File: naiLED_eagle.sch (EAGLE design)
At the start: 8 parts, among them IC1 TCS3414, U2 24LC00T-I/OT, U3 ATTINY25-20SSU

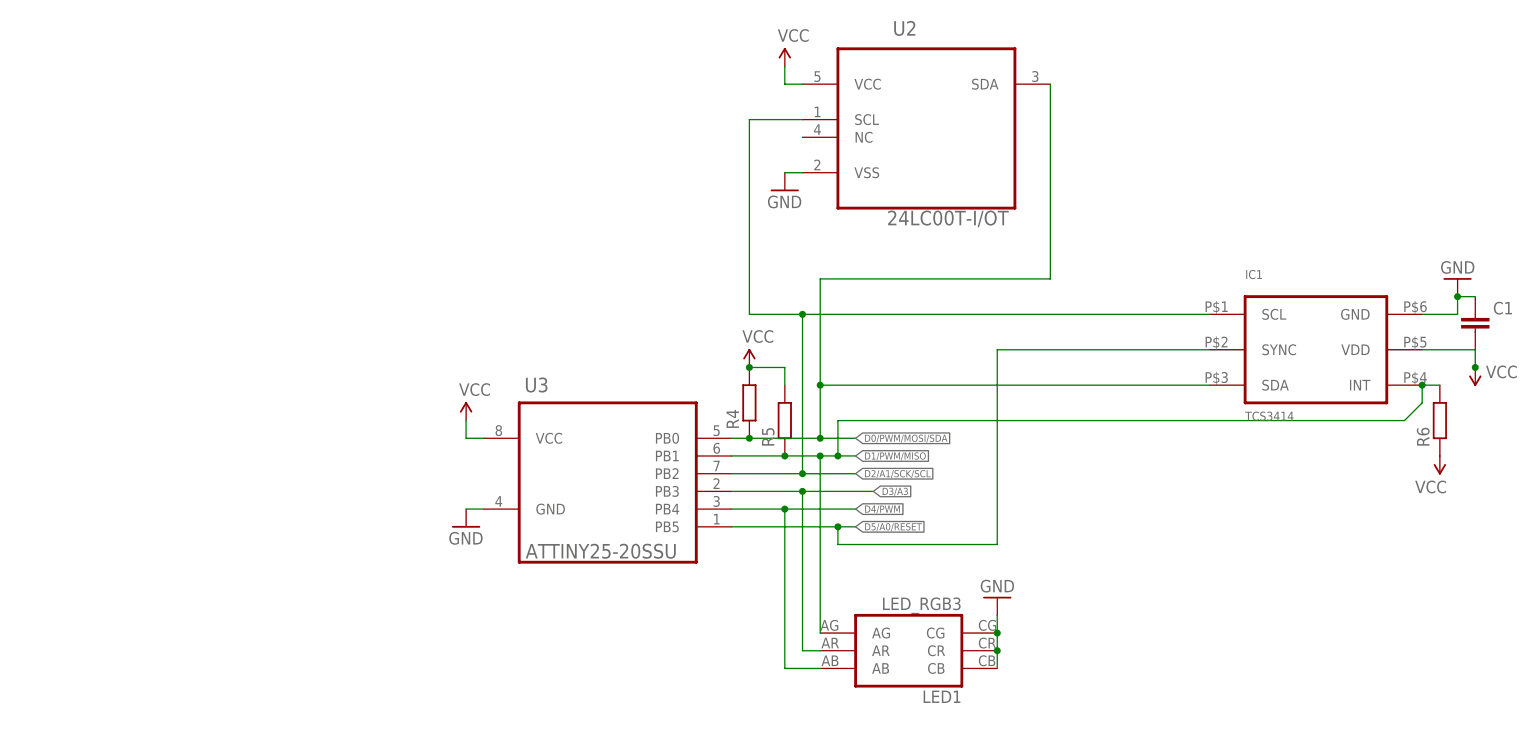
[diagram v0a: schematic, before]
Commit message: added library
ripup all , changed LED to CLPP4 and added resistors
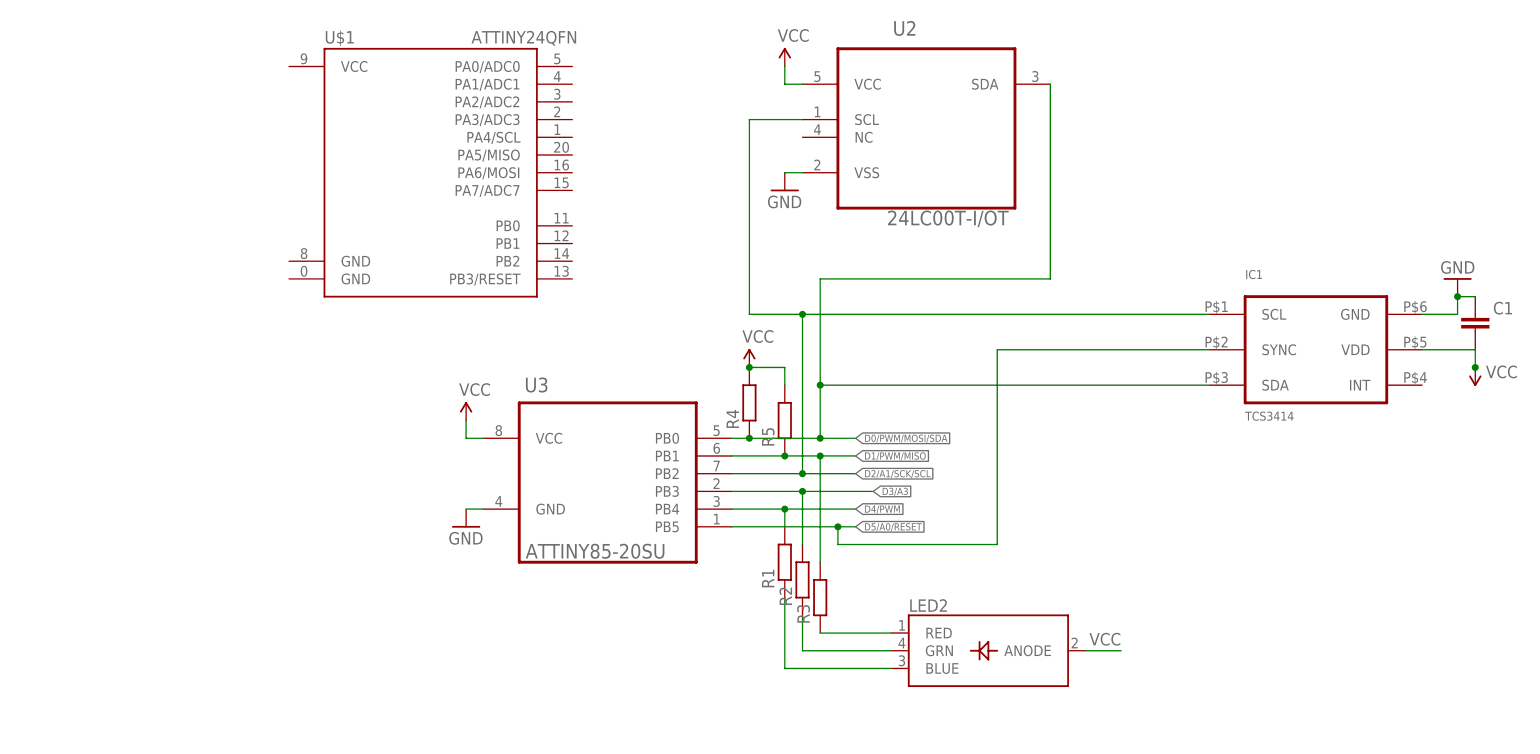
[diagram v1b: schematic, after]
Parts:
- removed LED1: LED_RGB3, dp_devices:LED_RGB3
- removed R6: (no value), dp_devices:RESISTOR-0402
- added LED2: (no value), microbuilder:LED_RGB_PLCC4
- added R1, R2, R3: (no value), dp_devices:RESISTOR-0402
- added U$1: ATTINY24QFN, SparkFun-DigitalIC:ATTINY24QFN
- U3: value ATTINY25-20SSU -> ATTINY85-20SU; device yair_r:ATTINY25-20SSU -> nld:ATTINY85-20SU
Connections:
- new net N$1: LED2.RED, R3.1
- new net N$2: LED2.GRN, R2.1
- new net N$3: LED2.BLUE, R1.1
- net D1/PWM/MISO: now also R3.2; no longer IC1.INT, LED1.AG, R6.2
- net D3/A3: now also R2.2; no longer LED1.AR
- net D4/PWM: now also R1.2; no longer LED1.AB
- net GND: no longer LED1.CB, LED1.CG, LED1.CR
- net VCC: now also LED2.ANODE; no longer R6.1
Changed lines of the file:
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@@
 <?xml version="1.0" encoding="utf-8"?>
 <!DOCTYPE eagle SYSTEM "eagle.dtd">
-<eagle version="6.4">
+<eagle version="7.1.0">
 <drawing>
 <settings>
@@
 <layer number="54" name="bGND_GNDA" color="7" fill="1" visible="no" active="no"/>
 <layer number="56" name="wert" color="7" fill="1" visible="no" active="no"/>
+<layer number="90" name="Modules" color="5" fill="1" visible="yes" active="yes"/>
 <layer number="91" name="Nets" color="2" fill="1" visible="yes" active="yes"/>
 <layer number="92" name="Busses" color="1" fill="1" visible="yes" active="yes"/>
@@
 <layer number="107" name="BD-Top" color="7" fill="1" visible="yes" active="yes"/>
 <layer number="108" name="centerline" color="7" fill="1" visible="yes" active="yes"/>
+<layer number="109" name="tBPL" color="7" fill="1" visible="yes" active="yes"/>
+<layer number="110" name="bBPL" color="7" fill="1" visible="yes" active="yes"/>
+<layer number="111" name="MPL" color="7" fill="1" visible="yes" active="yes"/>
+<layer number="112" name="tSilk" color="7" fill="1" visible="yes" active="yes"/>
 <layer number="116" name="Patch_BOT" color="7" fill="1" visible="yes" active="yes"/>
+<layer number="118" name="Rect_Pads" color="7" fill="1" visible="no" active="no"/>
 <layer number="121" name="_tsilk" color="7" fill="1" visible="yes" active="yes"/>
 <layer number="122" name="_bsilk" color="7" fill="1" visible="yes" active="yes"/>
+<layer number="123" name="tTestmark" color="7" fill="1" visible="no" active="yes"/>
+<layer number="124" name="bTestmark" color="7" fill="1" visible="no" active="yes"/>
 <layer number="125" name="_tNames" color="7" fill="1" visible="yes" active="yes"/>
+<layer number="126" name="_bNames" color="7" fill="1" visible="yes" active="yes"/>
+<layer number="127" name="_tValues" color="7" fill="1" visible="yes" active="yes"/>
+<layer number="128" name="_bValues" color="7" fill="1" visible="yes" active="yes"/>
 <layer number="131" name="prix" color="7" fill="1" visible="yes" active="yes"/>
 <layer number="132" name="test" color="7" fill="1" visible="yes" active="yes"/>
 <layer number="144" name="Drill_legend" color="7" fill="1" visible="yes" active="yes"/>
 <layer number="151" name="HeatSink" color="7" fill="1" visible="yes" active="yes"/>
+<layer number="152" name="_bDocu" color="7" fill="1" visible="yes" active="yes"/>
 <layer number="199" name="Contour" color="7" fill="1" visible="yes" active="yes"/>
 <layer number="200" name="200bmp" color="7" fill="1" visible="yes" active="yes"/>
@@
 <layer number="223" name="223bmp" color="24" fill="1" visible="no" active="no"/>
 <layer number="224" name="224bmp" color="25" fill="1" visible="no" active="no"/>
+<layer number="248" name="Housing" color="7" fill="1" visible="yes" active="yes"/>
+<layer number="249" name="Edge" color="7" fill="1" visible="yes" active="yes"/>
 <layer number="250" name="Descript" color="7" fill="1" visible="yes" active="yes"/>
 <layer number="251" name="SMDround" color="7" fill="1" visible="yes" active="yes"/>
@@
 <parts>
 <part name="U2" library="Microchip-24LCxxx" deviceset="24LC00T-I/OT" device=""/>
-<part name="U3" library="yair_r" deviceset="ATTINY25-20SSU" device=""/>
-<part name="LED1" library="dp_devices" deviceset="LED_RGB3" device=""/>
-<part name="GND1" library="SparkFun" deviceset="GND" device=""/>
+<part name="U3" library="nld" deviceset="ATTINY85-20SU" device=""/>
 <part name="GND3" library="SparkFun" deviceset="GND" device=""/>
 <part name="P+1" library="SparkFun" deviceset="VCC" device=""/>
@@
 <part name="R4" library="dp_devices" deviceset="RESISTOR" device="-0402"/>
 <part name="R5" library="dp_devices" deviceset="RESISTOR" device="-0402"/>
-<part name="P+5" library="SparkFun" deviceset="VCC" device=""/>
-<part name="R6" library="dp_devices" deviceset="RESISTOR" device="-0402"/>
 <part name="C1" library="dp_devices" deviceset="CAPACITOR_NPOL" device="-0402"/>
+<part name="LED2" library="microbuilder" deviceset="LED_RGB_PLCC4" device=""/>
+<part name="R1" library="dp_devices" deviceset="RESISTOR" device="-0402"/>
+<part name="R2" library="dp_devices" deviceset="RESISTOR" device="-0402"/>
+<part name="R3" library="dp_devices" deviceset="RESISTOR" device="-0402"/>
+<part name="U$1" library="SparkFun-DigitalIC" deviceset="ATTINY24" device="QFN"/>
 </parts>
 <sheets>
@@
 <attribute name="VALUE" x="-11.7856" y="13.2334" size="2.0828" layer="96" ratio="10" rot="SR0"/>
 </instance>
-<instance part="LED1" gate="G$1" x="43.18" y="0" rot="R180"/>
-<instance part="GND1" gate="1" x="55.88" y="7.62" rot="R180"/>
 <instance part="GND3" gate="1" x="-20.32" y="17.78"/>
 <instance part="P+1" gate="1" x="-20.32" y="33.02"/>
@@
 <instance part="R4" gate="G$1" x="20.32" y="35.56" rot="R90"/>
 <instance part="R5" gate="G$1" x="25.4" y="33.02" rot="R90"/>
-<instance part="P+5" gate="1" x="119.38" y="27.94" rot="R180"/>
-<instance part="R6" gate="G$1" x="119.38" y="33.02" rot="R90"/>
 <instance part="C1" gate="C" x="124.46" y="48.26" smashed="yes" rot="R180">
 <attribute name="NAME" x="127" y="48.26" size="1.778" layer="95"/>
 <attribute name="VALUE" x="121.92" y="45.72" size="1.778" layer="96" rot="R180"/>
 </instance>
+<instance part="LED2" gate="G$1" x="53.34" y="0"/>
+<instance part="R1" gate="G$1" x="25.4" y="12.7" rot="R90"/>
+<instance part="R2" gate="G$1" x="27.94" y="10.16" rot="R90"/>
+<instance part="R3" gate="G$1" x="30.48" y="7.62" rot="R90"/>
+<instance part="U$1" gate="G$1" x="-25.4" y="68.58"/>
 </instances>
 <busses>
@@
 </segment>
 <segment>
-<pinref part="R6" gate="G$1" pin="1"/>
-<pinref part="P+5" gate="1" pin="VCC"/>
+<wire x1="68.58" y1="0" x2="73.66" y2="0" width="0.1524" layer="91"/>
+<pinref part="LED2" gate="G$1" pin="ANODE"/>
+<label x="73.66" y="2.54" size="1.778" layer="95" rot="R180"/>
 </segment>
 </net>
 <net name="GND" class="0">
-<segment>
-<wire x1="55.88" y1="-2.54" x2="55.88" y2="0" width="0.1524" layer="91"/>
-<wire x1="55.88" y1="0" x2="55.88" y2="2.54" width="0.1524" layer="91"/>
-<wire x1="55.88" y1="2.54" x2="55.88" y2="5.08" width="0.1524" layer="91"/>
-<junction x="55.88" y="2.54"/>
-<junction x="55.88" y="0"/>
-<pinref part="GND1" gate="1" pin="GND"/>
-<pinref part="LED1" gate="G$1" pin="CB"/>
-<pinref part="LED1" gate="G$1" pin="CR"/>
-<pinref part="LED1" gate="G$1" pin="CG"/>
-</segment>
 <segment>
 <pinref part="GND3" gate="1" pin="GND"/>
@@
 <wire x1="17.78" y1="20.32" x2="25.4" y2="20.32" width="0.1524" layer="91"/>
 <junction x="25.4" y="20.32"/>
-<wire x1="25.4" y1="20.32" x2="25.4" y2="-2.54" width="0.1524" layer="91"/>
-<pinref part="LED1" gate="G$1" pin="AB"/>
-<wire x1="25.4" y1="-2.54" x2="30.48" y2="-2.54" width="0.1524" layer="91"/>
+<wire x1="25.4" y1="20.32" x2="25.4" y2="17.78" width="0.1524" layer="91"/>
+<pinref part="R1" gate="G$1" pin="2"/>
 </segment>
 </net>
@@
 <wire x1="27.94" y1="22.86" x2="38.1" y2="22.86" width="0.1524" layer="91"/>
 <junction x="27.94" y="22.86"/>
-<wire x1="27.94" y1="22.86" x2="27.94" y2="0" width="0.1524" layer="91"/>
-<pinref part="LED1" gate="G$1" pin="AR"/>
-<wire x1="30.48" y1="0" x2="27.94" y2="0" width="0.1524" layer="91"/>
+<wire x1="27.94" y1="22.86" x2="27.94" y2="15.24" width="0.1524" layer="91"/>
+<pinref part="R2" gate="G$1" pin="2"/>
 </segment>
 </net>
@@
 <label x="35.56" y="27.94" size="1.016" layer="95" xref="yes"/>
 <wire x1="25.4" y1="27.94" x2="30.48" y2="27.94" width="0.1524" layer="91"/>
-<wire x1="30.48" y1="27.94" x2="33.02" y2="27.94" width="0.1524" layer="91"/>
-<wire x1="33.02" y1="27.94" x2="35.56" y2="27.94" width="0.1524" layer="91"/>
-<wire x1="30.48" y1="27.94" x2="30.48" y2="2.54" width="0.1524" layer="91"/>
+<wire x1="30.48" y1="27.94" x2="35.56" y2="27.94" width="0.1524" layer="91"/>
+<wire x1="30.48" y1="27.94" x2="30.48" y2="12.7" width="0.1524" layer="91"/>
 <junction x="30.48" y="27.94"/>
 <pinref part="R5" gate="G$1" pin="1"/>
 <junction x="25.4" y="27.94"/>
-<pinref part="LED1" gate="G$1" pin="AG"/>
-<pinref part="IC1" gate="A" pin="INT"/>
-<wire x1="116.84" y1="38.1" x2="119.38" y2="38.1" width="0.1524" layer="91"/>
-<pinref part="R6" gate="G$1" pin="2"/>
-<wire x1="116.84" y1="38.1" x2="116.84" y2="35.56" width="0.1524" layer="91"/>
-<junction x="116.84" y="38.1"/>
-<wire x1="116.84" y1="35.56" x2="114.3" y2="33.02" width="0.1524" layer="91"/>
-<wire x1="114.3" y1="33.02" x2="33.02" y2="33.02" width="0.1524" layer="91"/>
-<wire x1="33.02" y1="33.02" x2="33.02" y2="27.94" width="0.1524" layer="91"/>
-<junction x="33.02" y="27.94"/>
+<pinref part="R3" gate="G$1" pin="2"/>
 </segment>
 </net>
@@
 </segment>
 </net>
+<net name="N$1" class="0">
+<segment>
+<pinref part="R3" gate="G$1" pin="1"/>
+<pinref part="LED2" gate="G$1" pin="RED"/>
+<wire x1="40.64" y1="2.54" x2="30.48" y2="2.54" width="0.1524" layer="91"/>
+</segment>
+</net>
+<net name="N$2" class="0">
+<segment>
+<pinref part="R2" gate="G$1" pin="1"/>
+<wire x1="27.94" y1="5.08" x2="27.94" y2="0" width="0.1524" layer="91"/>
+<pinref part="LED2" gate="G$1" pin="GRN"/>
+<wire x1="40.64" y1="0" x2="27.94" y2="0" width="0.1524" layer="91"/>
+</segment>
+</net>
+<net name="N$3" class="0">
+<segment>
+<pinref part="LED2" gate="G$1" pin="BLUE"/>
+<pinref part="R1" gate="G$1" pin="1"/>
+<wire x1="25.4" y1="7.62" x2="25.4" y2="-2.54" width="0.1524" layer="91"/>
+<wire x1="25.4" y1="-2.54" x2="40.64" y2="-2.54" width="0.1524" layer="91"/>
+</segment>
+</net>

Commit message: working on the at841
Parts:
- removed U$1: ATTINY24QFN, SparkFun-DigitalIC:ATTINY24QFN
- removed U3: ATTINY85-20SU, nld:ATTINY85-20SU
- added GND-TAB, VCC-TAB: (no value), adafruit:PINHD-1X1CB
- added IC2: ATTINY441/841-MU, nld:ATTINY441/841-MU
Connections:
- removed net D0/PWM/MOSI/SDA: IC1.SDA, R4.1, U2.SDA, U3.PB0
- removed net D1/PWM/MISO: R3.2, R5.1, U3.PB1
- removed net D2/A1/SCK/SCL: IC1.SCL, U2.SCL, U3.PB2
- removed net D3/A3: R2.2, U3.PB3
- removed net D4/PWM: R1.2, U3.PB4
- new net MISO: IC2.(PCINT0/ADC0/AREF/MISO)PA0, R5.1
- new net MOSI: IC1.SDA, IC2.(PCINT1/ADC1/AIN00/TOCC0/TXD0/MOSI)PA1, R4.1, U2.SDA
- new net N$4: IC2.(PCINT7/ADC7/TOCC6/ICP1/TXD0/SS)PA7, R1.2
- new net N$5: IC2.(PCINT6/ADC6/ACO1/TOCC5/XCK1/SDA/MOSI)PA6, R2.2
- new net N$6: IC2.(PCINT5/ADC5/ACO0/TOCC4/T2/TXD1/MISO)PA5, R3.2
- new net SCL: IC1.SCL, IC2.(PCINT4/ADC4/AIN11/TOCC3/T1/RXD1/SCL/SCK)PA4, U2.SCL
- net D5/A0/RESET: no longer U3.PB5
- net GND: now also GND-TAB.1, IC2.GND; no longer U3.GND
- net VCC: now also IC2.VCC, VCC-TAB.1; no longer U3.VCC
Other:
- note added: "find me home"
- moved on the sheet: LED2, R1, R2, R3, R4, R5

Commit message: some changes, nothing major
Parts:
- removed GND-TAB, VCC-TAB: (no value), adafruit:PINHD-1X1CB
- removed IC2: ATTINY441/841-MU, nld:ATTINY441/841-MU
- added U$1: ATTINY24QFN, SparkFun-DigitalIC:ATTINY24QFN
- added U3: ATTINY85-20SU, nld:ATTINY85-20SU
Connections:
- removed net MISO: IC2.(PCINT0/ADC0/AREF/MISO)PA0, R5.1
- removed net MOSI: IC1.SDA, IC2.(PCINT1/ADC1/AIN00/TOCC0/TXD0/MOSI)PA1, R4.1, U2.SDA
- removed net N$4: IC2.(PCINT7/ADC7/TOCC6/ICP1/TXD0/SS)PA7, R1.2
- removed net N$5: IC2.(PCINT6/ADC6/ACO1/TOCC5/XCK1/SDA/MOSI)PA6, R2.2
- removed net N$6: IC2.(PCINT5/ADC5/ACO0/TOCC4/T2/TXD1/MISO)PA5, R3.2
- removed net SCL: IC1.SCL, IC2.(PCINT4/ADC4/AIN11/TOCC3/T1/RXD1/SCL/SCK)PA4, U2.SCL
- new net D0/PWM/MOSI/SDA: IC1.SDA, R4.1, U2.SDA, U3.PB0
- new net D1/PWM/MISO: R3.2, R5.1, U3.PB1
- new net D2/A1/SCK/SCL: IC1.SCL, U2.SCL, U3.PB2
- new net D3/A3: R2.2, U3.PB3
- new net D4/PWM: R1.2, U3.PB4
- net D5/A0/RESET: now also U3.PB5
- net GND: now also U3.GND; no longer GND-TAB.1, IC2.GND
- net VCC: now also U3.VCC; no longer IC2.VCC, VCC-TAB.1
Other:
- note removed: "find me home"
- moved on the sheet: LED2, R1, R2, R3, R4, R5
